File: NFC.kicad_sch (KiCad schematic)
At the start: 2 parts

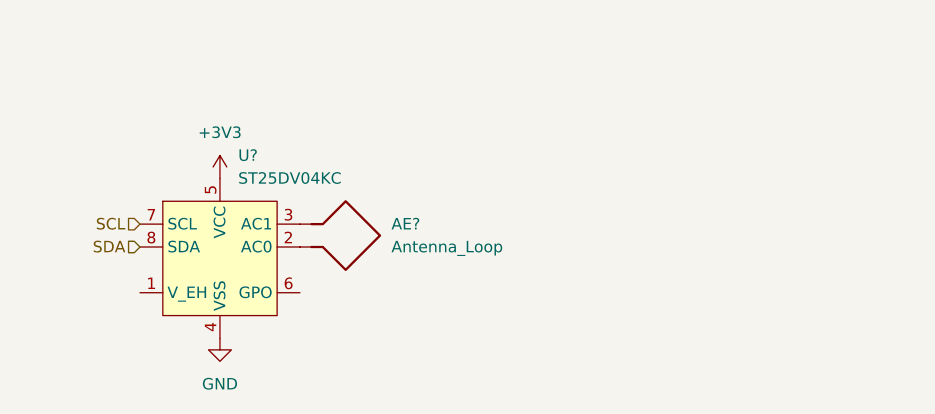
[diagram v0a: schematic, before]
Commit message: Added new lora, added rgb leds, updated TSP65988 schematic, added bat to 3v3, added battery balancer
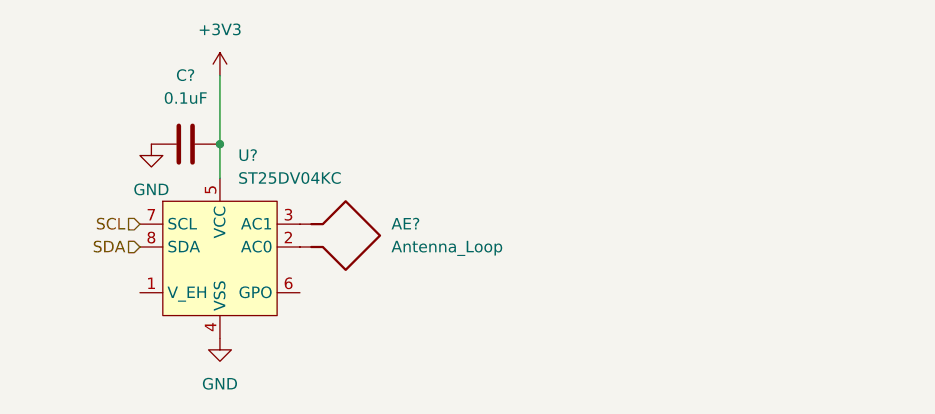
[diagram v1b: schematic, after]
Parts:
- added C?: 0.1uF, symbol Device:C
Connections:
- net +3V3: now also C?.2
- net GND: now also C?.1
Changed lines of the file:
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@@
 (kicad_sch (version 20211123) (generator eeschema)
   (paper "A4")
+  (junction (at 140.97 69.85) (diameter 0) (color 0 0 0 0)
+  )
+  (wire (pts (xy 140.97 69.85) (xy 140.97 73.66))
+    (stroke (width 0) (type default) (color 0 0 0 0))
+  )
+  (wire (pts (xy 140.97 62.23) (xy 140.97 69.85))
+    (stroke (width 0) (type default) (color 0 0 0 0))
+  )
   (hierarchical_label "SCL" (shape input) (at 132.08 78.74 180)
     (effects (font (size 1.27 1.27)) (justify right))
@@
   (hierarchical_label "SDA" (shape input) (at 132.08 81.28 180)
     (effects (font (size 1.27 1.27)) (justify right))
+  )
+  (symbol (lib_id "power:GND") (at 133.35 69.85 0) (unit 1)
+    (in_bom yes) (on_board yes) (fields_autoplaced)
+    (property "Reference" "#PWR?" (id 0) (at 133.35 76.2 0)
+      (effects (font (size 1.27 1.27)) hide)
+    )
+    (property "Value" "GND" (id 1) (at 133.35 74.93 0))
+    (property "Footprint" "" (id 2) (at 133.35 69.85 0)
+      (effects (font (size 1.27 1.27)) hide)
+    )
+    (property "Datasheet" "" (id 3) (at 133.35 69.85 0)
+      (effects (font (size 1.27 1.27)) hide)
+    )
+    (pin "1")
   )
   (symbol (lib_id "power:GND") (at 140.97 91.44 0) (unit 1)
@@
     (pin "1")
   )
-  (symbol (lib_id "power:+3V3") (at 140.97 73.66 0) (unit 1)
+  (symbol (lib_id "power:+3V3") (at 140.97 62.23 0) (unit 1)
     (in_bom yes) (on_board yes) (fields_autoplaced)
-    (property "Reference" "#PWR?" (id 0) (at 140.97 77.47 0)
+    (property "Reference" "#PWR?" (id 0) (at 140.97 66.04 0)
       (effects (font (size 1.27 1.27)) hide)
     )
-    (property "Value" "+3V3" (id 1) (at 140.97 68.58 0))
-    (property "Footprint" "" (id 2) (at 140.97 73.66 0)
+    (property "Value" "+3V3" (id 1) (at 140.97 57.15 0))
+    (property "Footprint" "" (id 2) (at 140.97 62.23 0)
       (effects (font (size 1.27 1.27)) hide)
     )
-    (property "Datasheet" "" (id 3) (at 140.97 73.66 0)
+    (property "Datasheet" "" (id 3) (at 140.97 62.23 0)
       (effects (font (size 1.27 1.27)) hide)
     )
@@
     (pin "8")
   )
+  (symbol (lib_id "Device:C") (at 137.16 69.85 90) (unit 1)
+    (in_bom yes) (on_board yes) (fields_autoplaced)
+    (property "Reference" "C?" (id 0) (at 137.16 62.23 90))
+    (property "Value" "0.1uF" (id 1) (at 137.16 64.77 90))
+    (property "Footprint" "" (id 2) (at 140.97 68.8848 0)
+      (effects (font (size 1.27 1.27)) hide)
+    )
+    (property "Datasheet" "~" (id 3) (at 137.16 69.85 0)
+      (effects (font (size 1.27 1.27)) hide)
+    )
+    (pin "1")
+    (pin "2")
+  )
 )

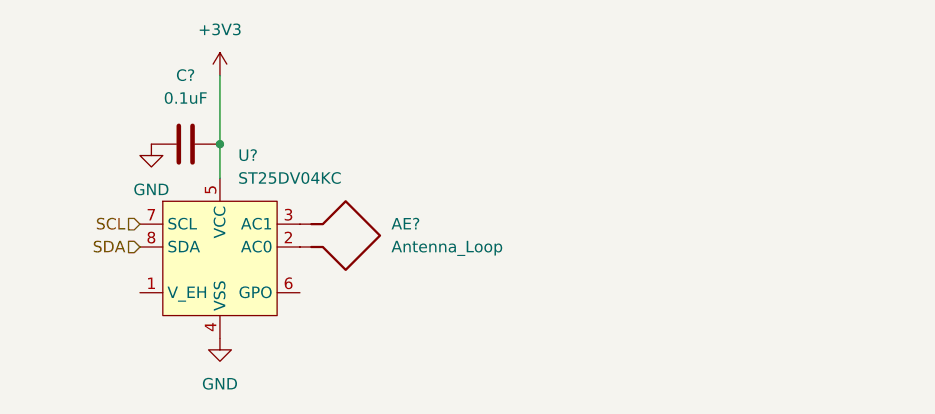
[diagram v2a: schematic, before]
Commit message: added audio ref schematic, added bat to 5V, added shift register, connected devices with other periferals
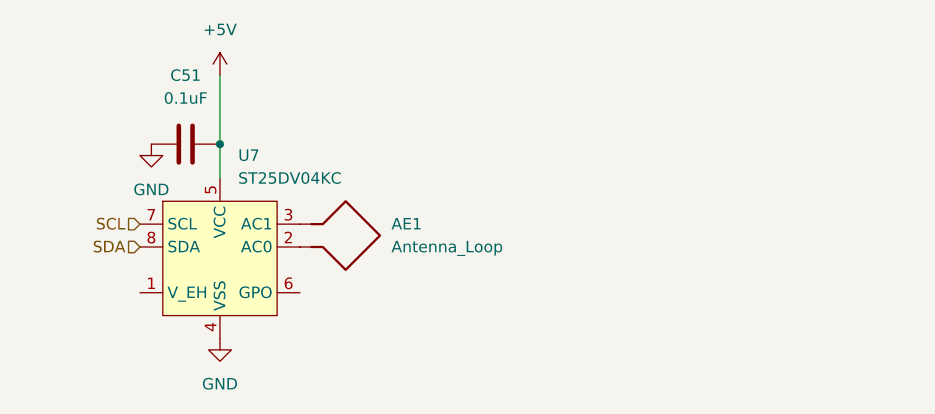
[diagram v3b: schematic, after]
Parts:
- gave numbers to parts that had none: 3
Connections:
- net +3V3 renamed +5V
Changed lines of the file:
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@@
-    (pin "1")
-  )
-  (symbol (lib_id "power:+3V3") (at 140.97 62.23 0) (unit 1)
-    (in_bom yes) (on_board yes) (fields_autoplaced)
-    (property "Reference" "#PWR0158" (id 0) (at 140.97 66.04 0)
-      (effects (font (size 1.27 1.27)) hide)
-    )
-    (property "Value" "+3V3" (id 1) (at 140.97 57.15 0))
-    (property "Footprint" "" (id 2) (at 140.97 62.23 0)
-      (effects (font (size 1.27 1.27)) hide)
-    )
-    (property "Datasheet" "" (id 3) (at 140.97 62.23 0)
-      (effects (font (size 1.27 1.27)) hide)
-    )
     (pin "1")
   )
   (symbol (lib_id "Device:Antenna_Loop") (at 154.94 78.74 270) (unit 1)
     (in_bom yes) (on_board yes) (fields_autoplaced)
-    (property "Reference" "AE?" (id 0) (at 160.02 78.7399 90)
+    (property "Reference" "AE1" (id 0) (at 160.02 78.7399 90)
       (effects (font (size 1.27 1.27)) (justify left))
     )
@@
     (pin "2")
   )
+  (symbol (lib_id "power:+5V") (at 140.97 62.23 0) (unit 1)
+    (in_bom yes) (on_board yes) (fields_autoplaced)
+    (property "Reference" "#PWR?" (id 0) (at 140.97 66.04 0)
+      (effects (font (size 1.27 1.27)) hide)
+    )
+    (property "Value" "+5V" (id 1) (at 140.97 57.15 0))
+    (property "Footprint" "" (id 2) (at 140.97 62.23 0)
+      (effects (font (size 1.27 1.27)) hide)
+    )
+    (property "Datasheet" "" (id 3) (at 140.97 62.23 0)
+      (effects (font (size 1.27 1.27)) hide)
+    )
+    (pin "1")
+  )
   (symbol (lib_id "airsoft_controller:ST25DV04KC") (at 140.97 82.55 0) (unit 1)
     (in_bom yes) (on_board yes) (fields_autoplaced)
-    (property "Reference" "U?" (id 0) (at 142.9894 71.12 0)
+    (property "Reference" "U7" (id 0) (at 142.9894 71.12 0)
       (effects (font (size 1.27 1.27)) (justify left))
     )
@@
   (symbol (lib_id "Device:C") (at 137.16 69.85 90) (unit 1)
     (in_bom yes) (on_board yes) (fields_autoplaced)
-    (property "Reference" "C?" (id 0) (at 137.16 62.23 90))
+    (property "Reference" "C51" (id 0) (at 137.16 62.23 90))
     (property "Value" "0.1uF" (id 1) (at 137.16 64.77 90))
     (property "Footprint" "" (id 2) (at 140.97 68.8848 0)

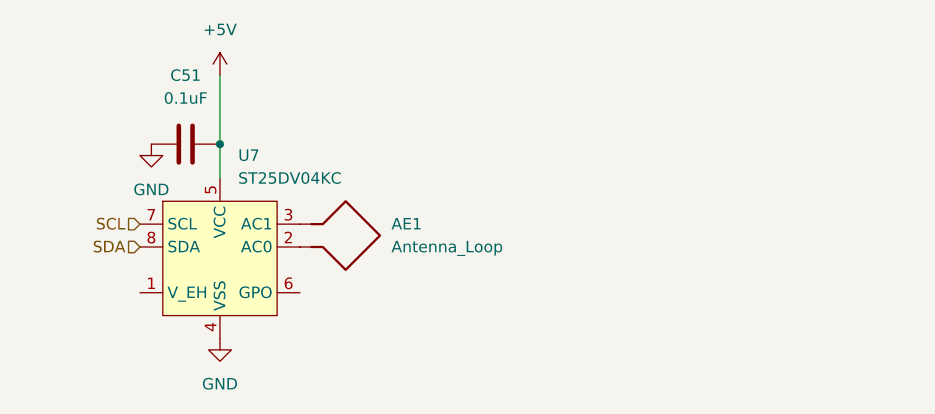
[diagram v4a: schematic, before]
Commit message: minor optimized pinassignement, added capacitors, added connectors
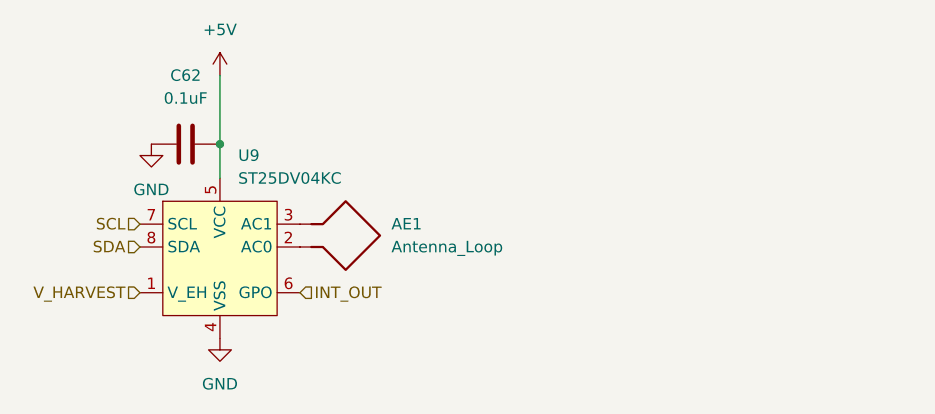
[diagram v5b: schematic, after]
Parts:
- renumbered C51 to C62, U7 to U9
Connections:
- net V_HARVEST: now reaches U9.1 (V_EH)
- net INT_OUT: now reaches U9.6 (GPO)
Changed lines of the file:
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@@
     (stroke (width 0) (type default) (color 0 0 0 0))
+  )
+  (hierarchical_label "INT_OUT" (shape input) (at 149.86 86.36 0)
+    (effects (font (size 1.27 1.27)) (justify left))
   )
   (hierarchical_label "SCL" (shape input) (at 132.08 78.74 180)
@@
     (effects (font (size 1.27 1.27)) (justify right))
   )
+  (hierarchical_label "V_HARVEST" (shape input) (at 132.08 86.36 180)
+    (effects (font (size 1.27 1.27)) (justify right))
+  )
   (symbol (lib_id "power:GND") (at 133.35 69.85 0) (unit 1)
     (in_bom yes) (on_board yes) (fields_autoplaced)
-    (property "Reference" "#PWR0157" (id 0) (at 133.35 76.2 0)
+    (property "Reference" "#PWR074" (id 0) (at 133.35 76.2 0)
       (effects (font (size 1.27 1.27)) hide)
     )
@@
   (symbol (lib_id "power:GND") (at 140.97 91.44 0) (unit 1)
     (in_bom yes) (on_board yes) (fields_autoplaced)
-    (property "Reference" "#PWR0159" (id 0) (at 140.97 97.79 0)
+    (property "Reference" "#PWR076" (id 0) (at 140.97 97.79 0)
       (effects (font (size 1.27 1.27)) hide)
     )
@@
   (symbol (lib_id "power:+5V") (at 140.97 62.23 0) (unit 1)
     (in_bom yes) (on_board yes) (fields_autoplaced)
-    (property "Reference" "#PWR0263" (id 0) (at 140.97 66.04 0)
+    (property "Reference" "#PWR075" (id 0) (at 140.97 66.04 0)
       (effects (font (size 1.27 1.27)) hide)
     )
@@
   (symbol (lib_id "airsoft_controller:ST25DV04KC") (at 140.97 82.55 0) (unit 1)
     (in_bom yes) (on_board yes) (fields_autoplaced)
-    (property "Reference" "U7" (id 0) (at 142.9894 71.12 0)
+    (property "Reference" "U9" (id 0) (at 142.9894 71.12 0)
       (effects (font (size 1.27 1.27)) (justify left))
     )
@@
   (symbol (lib_id "Device:C") (at 137.16 69.85 90) (unit 1)
     (in_bom yes) (on_board yes) (fields_autoplaced)
-    (property "Reference" "C51" (id 0) (at 137.16 62.23 90))
+    (property "Reference" "C62" (id 0) (at 137.16 62.23 90))
     (property "Value" "0.1uF" (id 1) (at 137.16 64.77 90))
     (property "Footprint" "" (id 2) (at 140.97 68.8848 0)

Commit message: PI LC lowpass filter, added CP2012 reset, added connectors
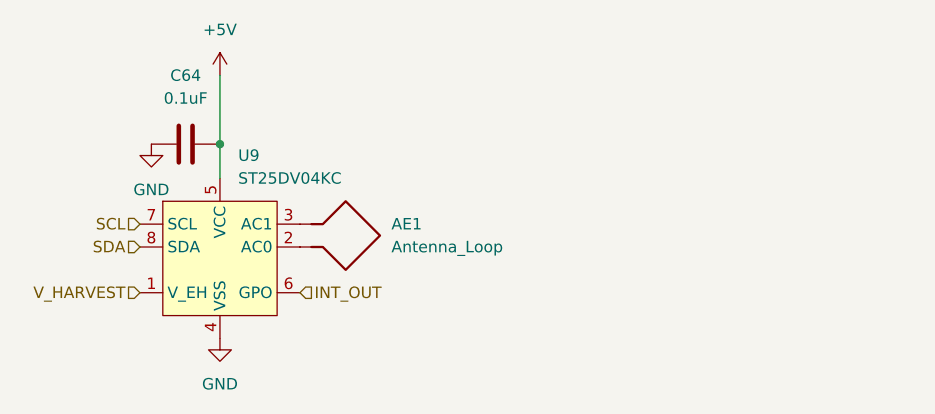
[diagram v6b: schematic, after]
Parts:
- renumbered C62 to C64
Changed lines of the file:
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@@
   (symbol (lib_id "power:GND") (at 133.35 69.85 0) (unit 1)
     (in_bom yes) (on_board yes) (fields_autoplaced)
-    (property "Reference" "#PWR074" (id 0) (at 133.35 76.2 0)
+    (property "Reference" "#PWR073" (id 0) (at 133.35 76.2 0)
       (effects (font (size 1.27 1.27)) hide)
     )
@@
   (symbol (lib_id "power:GND") (at 140.97 91.44 0) (unit 1)
     (in_bom yes) (on_board yes) (fields_autoplaced)
-    (property "Reference" "#PWR076" (id 0) (at 140.97 97.79 0)
+    (property "Reference" "#PWR075" (id 0) (at 140.97 97.79 0)
       (effects (font (size 1.27 1.27)) hide)
     )
@@
   (symbol (lib_id "power:+5V") (at 140.97 62.23 0) (unit 1)
     (in_bom yes) (on_board yes) (fields_autoplaced)
-    (property "Reference" "#PWR075" (id 0) (at 140.97 66.04 0)
+    (property "Reference" "#PWR074" (id 0) (at 140.97 66.04 0)
       (effects (font (size 1.27 1.27)) hide)
     )
@@
   (symbol (lib_id "Device:C") (at 137.16 69.85 90) (unit 1)
     (in_bom yes) (on_board yes) (fields_autoplaced)
-    (property "Reference" "C62" (id 0) (at 137.16 62.23 90))
+    (property "Reference" "C64" (id 0) (at 137.16 62.23 90))
     (property "Value" "0.1uF" (id 1) (at 137.16 64.77 90))
     (property "Footprint" "" (id 2) (at 140.97 68.8848 0)
